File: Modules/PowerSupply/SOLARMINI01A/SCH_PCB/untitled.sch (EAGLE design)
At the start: 28 parts, among them X2 SROUB3M, X3 SROUB3M, X4 SROUB3M, X5 SROUB3M

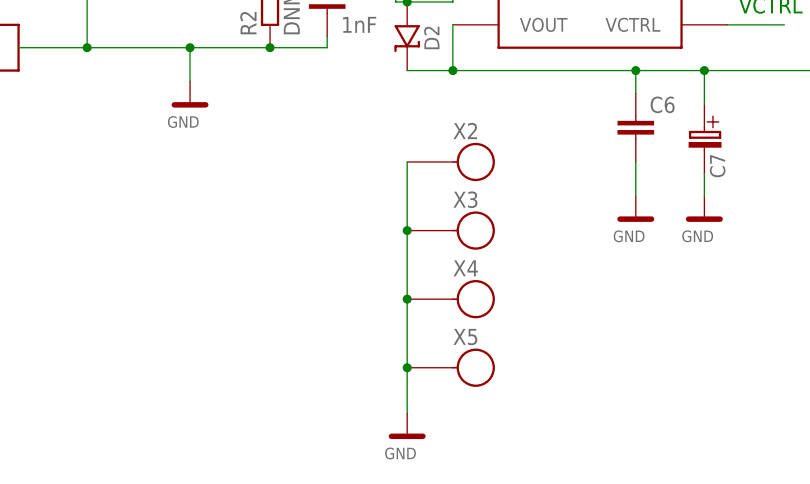
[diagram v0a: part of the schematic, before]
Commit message: 
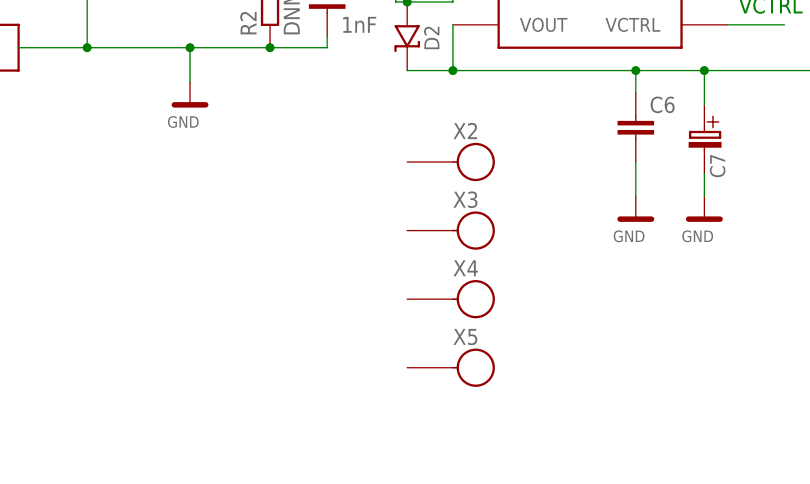
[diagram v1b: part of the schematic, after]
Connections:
- net GND: no longer X2.P$1, X3.P$1, X4.P$1, X5.P$1
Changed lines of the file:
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@@
 <?xml version="1.0" encoding="utf-8"?>
 <!DOCTYPE eagle SYSTEM "eagle.dtd">
-<eagle version="6.2">
+<eagle version="6.1">
 <drawing>
 <settings>
@@
 <part name="X4" library="moje" deviceset="SROUB3M" device=""/>
 <part name="X5" library="moje" deviceset="SROUB3M" device=""/>
-<part name="GND8" library="moje" deviceset="GND" device=""/>
 <part name="R6" library="moje_R" deviceset="R1206" device="" value="0R"/>
 <part name="R3" library="moje_R" deviceset="R1206" device="" value="0R"/>
@@
 <instance part="X4" gate="P4" x="-12.7" y="5.08"/>
 <instance part="X5" gate="P4" x="-12.7" y="-2.54"/>
-<instance part="GND8" gate="G$1" x="-20.32" y="-7.62"/>
 <instance part="R6" gate="G$1" x="55.88" y="35.56"/>
 <instance part="R3" gate="G$1" x="0" y="60.96"/>
@@
 </segment>
 <segment>
-<pinref part="X2" gate="P4" pin="P$1"/>
-<wire x1="-20.32" y1="20.32" x2="-20.32" y2="12.7" width="0.1524" layer="91"/>
-<pinref part="X3" gate="P4" pin="P$1"/>
-<junction x="-20.32" y="12.7"/>
-<wire x1="-20.32" y1="12.7" x2="-20.32" y2="5.08" width="0.1524" layer="91"/>
-<pinref part="X4" gate="P4" pin="P$1"/>
-<junction x="-20.32" y="5.08"/>
-<wire x1="-20.32" y1="5.08" x2="-20.32" y2="-2.54" width="0.1524" layer="91"/>
-<pinref part="X5" gate="P4" pin="P$1"/>
-<junction x="-20.32" y="-2.54"/>
-<wire x1="-20.32" y1="-2.54" x2="-20.32" y2="-7.62" width="0.1524" layer="91"/>
-<pinref part="GND8" gate="G$1" pin="GND"/>
-</segment>
-<segment>

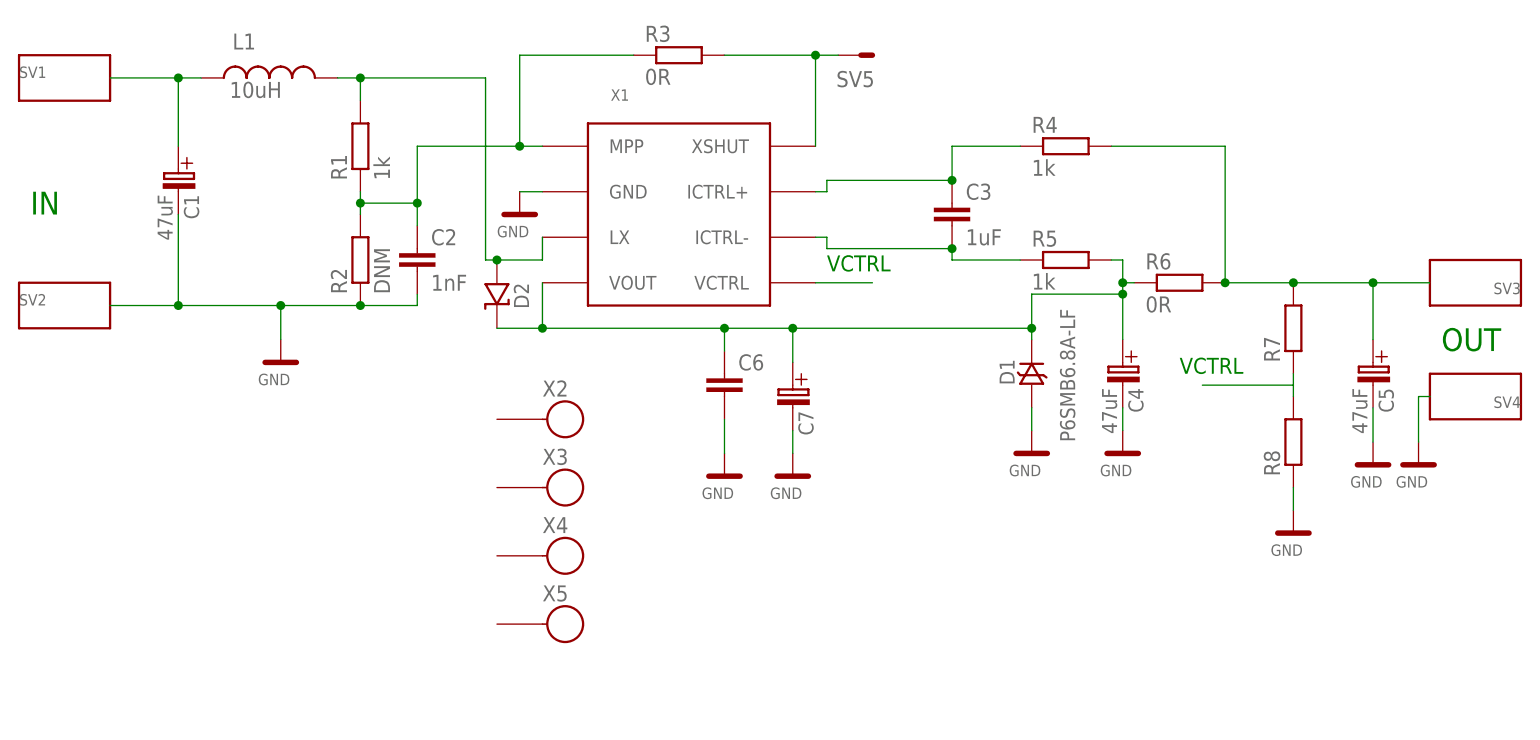
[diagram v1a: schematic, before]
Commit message: 
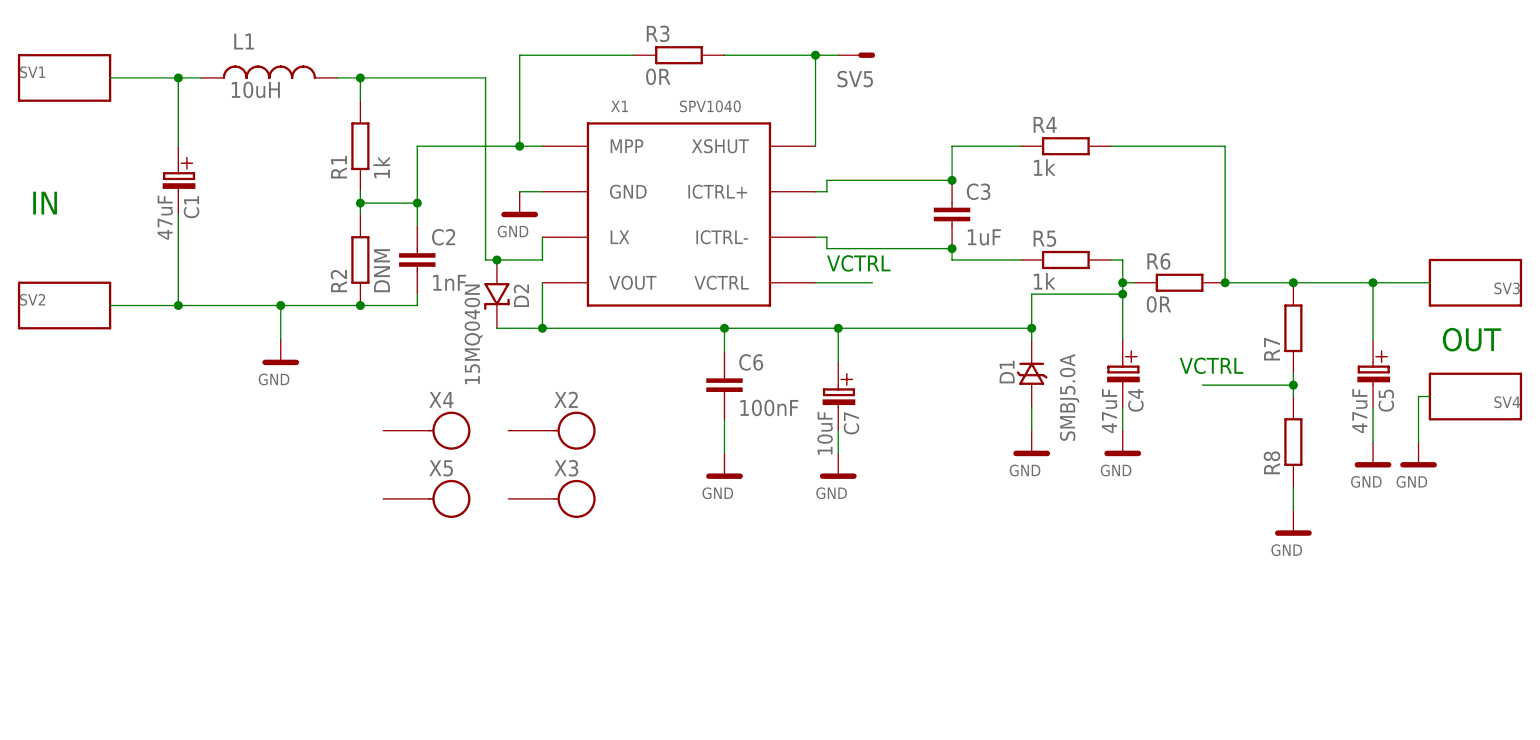
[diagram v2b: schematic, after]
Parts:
- C6: value (none) -> 100nF
- C7: value (none) -> 10uF
- D1: value P6SMB6.8A-LF -> SMBJ5.0A
- D2: value (none) -> 15MQ040N
- X1: value (none) -> SPV1040
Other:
- moved on the sheet: C7, X2, X3, X4, X5
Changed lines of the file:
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@@
 <setting verticaltext="up"/>
 </settings>
-<grid distance="0.1" unitdist="inch" unit="inch" style="lines" multiple="1" display="no" altdistance="0.01" altunitdist="inch" altunit="inch"/>
+<grid distance="0.05" unitdist="inch" unit="inch" style="lines" multiple="1" display="no" altdistance="0.01" altunitdist="inch" altunit="inch"/>
 <layers>
 <layer number="1" name="Top" color="4" fill="1" visible="no" active="no"/>
@@
 </classes>
 <parts>
-<part name="X1" library="moje_io" deviceset="SPV1040" device=""/>
+<part name="X1" library="moje_io" deviceset="SPV1040" device="" value="SPV1040"/>
 <part name="C1" library="moje_C" deviceset="C" device="" value="47uF"/>
 <part name="C2" library="moje_C" deviceset="C0805" device="" value="1nF"/>
@@
 <part name="R7" library="moje_R" deviceset="R0805" device=""/>
 <part name="R8" library="moje_R" deviceset="R0805" device=""/>
-<part name="D1" library="moje_diody" deviceset="D-TRANSIL" device="" value="P6SMB6.8A-LF"/>
+<part name="D1" library="moje_diody" deviceset="D-TRANSIL" device="" value="SMBJ5.0A"/>
 <part name="L1" library="moje_L" deviceset="DE1205-10" device="" value="10uH"/>
 <part name="SV1" library="moje_konektory" deviceset="WAGO256" device=""/>
@@
 <part name="R6" library="moje_R" deviceset="R1206" device="" value="0R"/>
 <part name="R3" library="moje_R" deviceset="R1206" device="" value="0R"/>
-<part name="D2" library="moje_diody" deviceset="D-SHOTKY-SMA" device=""/>
-<part name="C6" library="moje_C" deviceset="C0805" device=""/>
-<part name="C7" library="moje_C" deviceset="B" device=""/>
+<part name="D2" library="moje_diody" deviceset="D-SHOTKY-SMA" device="" value="15MQ040N"/>
+<part name="C6" library="moje_C" deviceset="C0805" device="" value="100nF"/>
+<part name="C7" library="moje_C" deviceset="B" device="" value="10uF"/>
 <part name="GND9" library="moje" deviceset="GND" device=""/>
 <part name="GND10" library="moje" deviceset="GND" device=""/>
@@
 </plain>
 <instances>
-<instance part="X1" gate="G$1" x="-5.08" y="45.72"/>
+<instance part="X1" gate="G$1" x="-5.08" y="45.72" smashed="yes">
+<attribute name="NAME" x="-7.62" y="54.61" size="1.27" layer="95"/>
+<attribute name="VALUE" x="0" y="54.61" size="1.27" layer="96"/>
+</instance>
 <instance part="C1" gate="G$1" x="-55.88" y="46.99" rot="R270"/>
 <instance part="C2" gate="G$1" x="-29.21" y="36.83"/>
@@
 <instance part="GND6" gate="G$1" x="77.47" y="17.78"/>
 <instance part="GND7" gate="G$1" x="82.55" y="17.78"/>
-<instance part="X2" gate="P4" x="-12.7" y="20.32"/>
-<instance part="X3" gate="P4" x="-12.7" y="12.7"/>
-<instance part="X4" gate="P4" x="-12.7" y="5.08"/>
-<instance part="X5" gate="P4" x="-12.7" y="-2.54"/>
+<instance part="X2" gate="P4" x="-11.43" y="19.05"/>
+<instance part="X3" gate="P4" x="-11.43" y="11.43"/>
+<instance part="X4" gate="P4" x="-25.4" y="19.05"/>
+<instance part="X5" gate="P4" x="-25.4" y="11.43"/>
 <instance part="R6" gate="G$1" x="55.88" y="35.56"/>
 <instance part="R3" gate="G$1" x="0" y="60.96"/>
 <instance part="D2" gate="G$1" x="-20.32" y="35.56" rot="R270"/>
 <instance part="C6" gate="G$1" x="5.08" y="22.86"/>
-<instance part="C7" gate="G$1" x="12.7" y="22.86" rot="R270"/>
+<instance part="C7" gate="G$1" x="17.78" y="22.86" rot="R270"/>
 <instance part="GND9" gate="G$1" x="5.08" y="16.51"/>
-<instance part="GND10" gate="G$1" x="12.7" y="16.51"/>
+<instance part="GND10" gate="G$1" x="17.78" y="16.51"/>
 <instance part="SV5" gate="G$1" x="17.78" y="60.96" rot="R180"/>
 </instances>
@@
 <pinref part="C7" gate="G$1" pin="C_EL-"/>
 <pinref part="GND10" gate="G$1" pin="GND"/>
-<wire x1="12.7" y1="16.51" x2="12.7" y2="19.05" width="0.1524" layer="91"/>
+<wire x1="17.78" y1="16.51" x2="17.78" y2="19.05" width="0.1524" layer="91"/>
 </segment>
 </net>
@@
 <wire x1="-15.24" y1="30.48" x2="5.08" y2="30.48" width="0.1524" layer="91"/>
 <pinref part="D1" gate="G$1" pin="K"/>
-<wire x1="5.08" y1="30.48" x2="12.7" y2="30.48" width="0.1524" layer="91"/>
-<wire x1="12.7" y1="30.48" x2="39.37" y2="30.48" width="0.1524" layer="91"/>
+<wire x1="5.08" y1="30.48" x2="17.78" y2="30.48" width="0.1524" layer="91"/>
+<wire x1="17.78" y1="30.48" x2="39.37" y2="30.48" width="0.1524" layer="91"/>
 <wire x1="39.37" y1="29.21" x2="39.37" y2="30.48" width="0.1524" layer="91"/>
 <pinref part="C4" gate="G$1" pin="C_EL+"/>
@@
 <wire x1="5.08" y1="27.94" x2="5.08" y2="30.48" width="0.1524" layer="91"/>
 <pinref part="C7" gate="G$1" pin="C_EL+"/>
-<wire x1="12.7" y1="26.67" x2="12.7" y2="30.48" width="0.1524" layer="91"/>
+<wire x1="17.78" y1="26.67" x2="17.78" y2="30.48" width="0.1524" layer="91"/>
 <junction x="5.08" y="30.48"/>
-<junction x="12.7" y="30.48"/>
+<junction x="17.78" y="30.48"/>
 </segment>
 </net>
@@
 <wire x1="68.58" y1="24.13" x2="68.58" y2="22.86" width="0.1524" layer="91"/>
 <wire x1="68.58" y1="24.13" x2="58.42" y2="24.13" width="0.1524" layer="91"/>
-</segment>
-</net>
+<junction x="68.58" y="24.13"/>
+</segment>
+</net>

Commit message: 
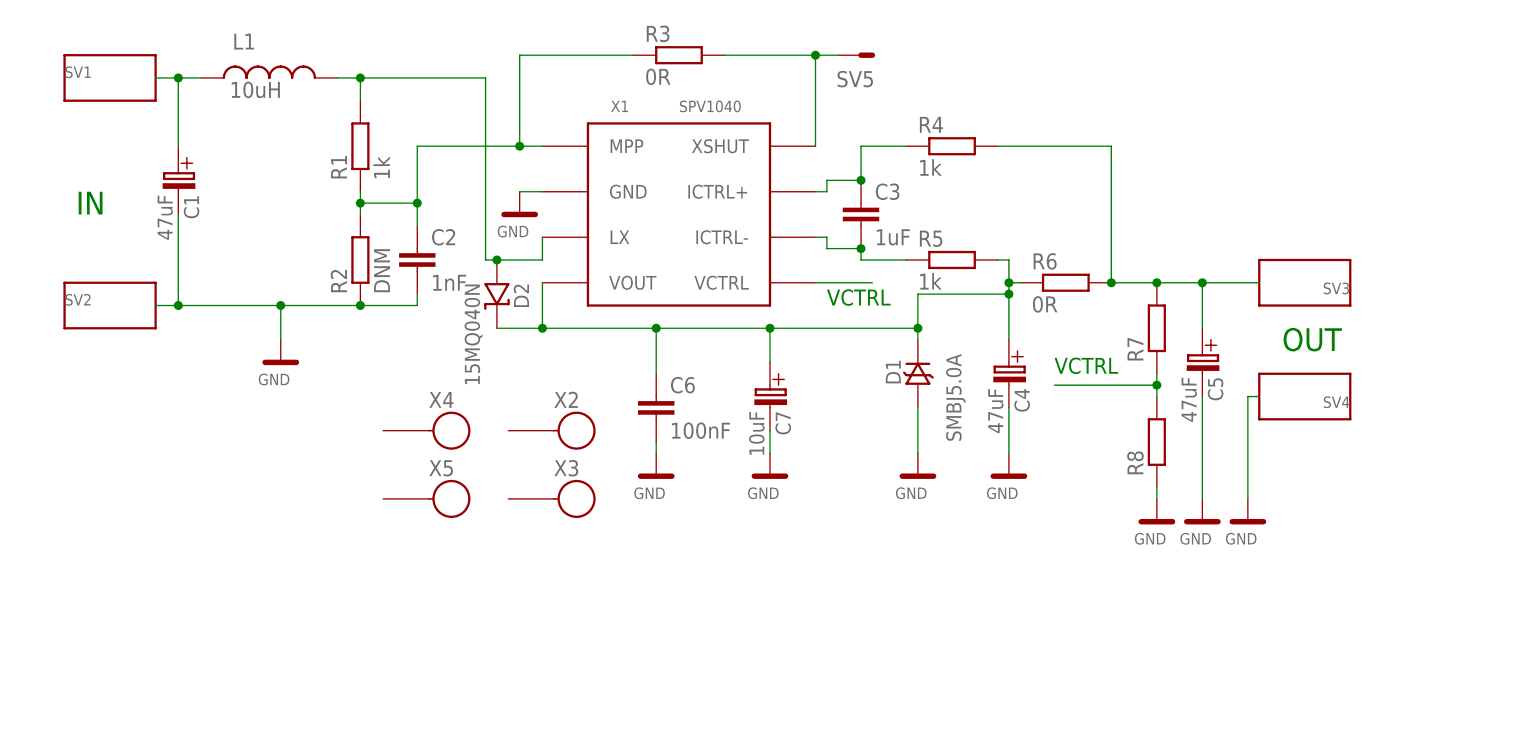
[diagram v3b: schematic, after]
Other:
- moved on the sheet: C3, C4, C5, C6, C7, D1, R4, R5, R6, R7, R8, SV1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

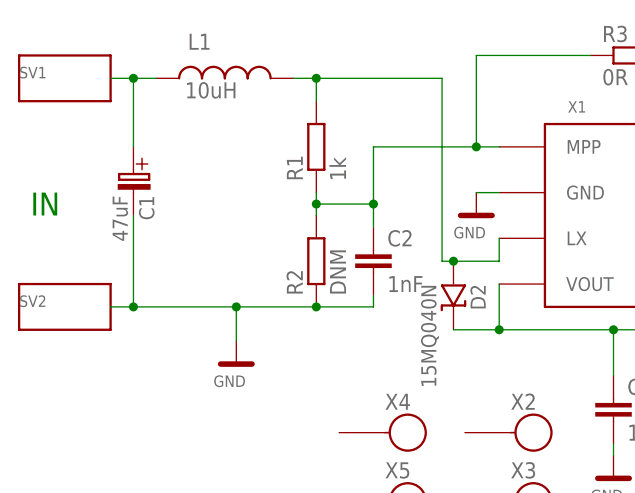
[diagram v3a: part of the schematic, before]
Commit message: 
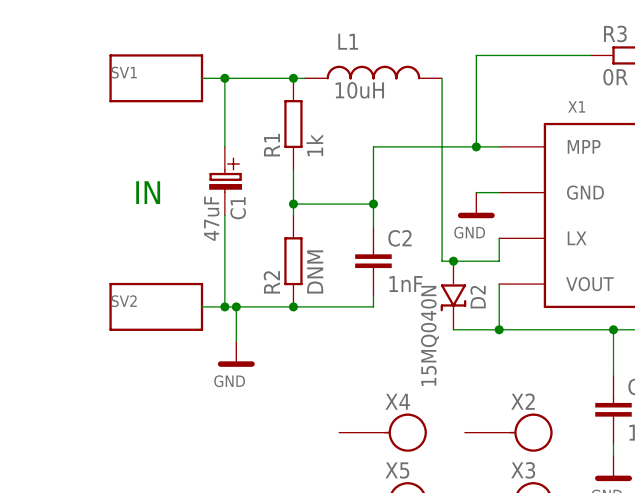
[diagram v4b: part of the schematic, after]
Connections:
- net N$1: now also R1.2
- net N$6: no longer R1.2
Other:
- moved on the sheet: C1, L1, R1, R2, SV1, SV2
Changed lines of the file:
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@@
 <text x="16.51" y="33.02" size="1.778" layer="91">VCTRL</text>
 <text x="41.91" y="25.4" size="1.778" layer="91">VCTRL</text>
-<text x="-67.31" y="43.18" size="2.54" layer="91">IN</text>
+<text x="-55.88" y="44.45" size="2.54" layer="91">IN</text>
 <text x="67.31" y="27.94" size="2.54" layer="91">OUT</text>
 </plain>
@@
 <attribute name="VALUE" x="0" y="54.61" size="1.27" layer="96"/>
 </instance>
-<instance part="C1" gate="G$1" x="-55.88" y="46.99" rot="R270"/>
+<instance part="C1" gate="G$1" x="-45.72" y="46.99" rot="R270"/>
 <instance part="C2" gate="G$1" x="-29.21" y="36.83"/>
 <instance part="C3" gate="G$1" x="20.32" y="41.91"/>
 <instance part="C4" gate="G$1" x="36.83" y="25.4" rot="R270"/>
 <instance part="C5" gate="G$1" x="58.42" y="26.67" rot="R270"/>
-<instance part="R1" gate="G$1" x="-35.56" y="50.8" rot="R90"/>
-<instance part="R2" gate="G$1" x="-35.56" y="38.1" rot="R90"/>
+<instance part="R1" gate="G$1" x="-38.1" y="53.34" rot="R90"/>
+<instance part="R2" gate="G$1" x="-38.1" y="38.1" rot="R90"/>
 <instance part="R4" gate="G$1" x="30.48" y="50.8"/>
 <instance part="R5" gate="G$1" x="30.48" y="38.1"/>
@@
 <attribute name="NAME" x="24.765" y="24.13" size="1.6764" layer="95" rot="R90"/>
 </instance>
-<instance part="L1" gate="G$1" x="-45.72" y="58.42"/>
-<instance part="SV1" gate="G$1" x="-66.04" y="58.42"/>
-<instance part="SV2" gate="G$1" x="-66.04" y="33.02"/>
+<instance part="L1" gate="G$1" x="-29.21" y="58.42"/>
+<instance part="SV1" gate="G$1" x="-55.88" y="58.42"/>
+<instance part="SV2" gate="G$1" x="-55.88" y="33.02"/>
 <instance part="SV3" gate="G$1" x="72.39" y="35.56" rot="R180"/>
 <instance part="SV4" gate="G$1" x="72.39" y="22.86" rot="R180"/>
@@
 <pinref part="SV1" gate="G$1" pin="P$1"/>
 <pinref part="L1" gate="G$1" pin="1"/>
-<wire x1="-58.42" y1="58.42" x2="-55.88" y2="58.42" width="0.1524" layer="91"/>
-<wire x1="-55.88" y1="58.42" x2="-53.34" y2="58.42" width="0.1524" layer="91"/>
-<wire x1="-55.88" y1="50.8" x2="-55.88" y2="58.42" width="0.1524" layer="91"/>
+<wire x1="-48.26" y1="58.42" x2="-45.72" y2="58.42" width="0.1524" layer="91"/>
+<wire x1="-45.72" y1="58.42" x2="-38.1" y2="58.42" width="0.1524" layer="91"/>
+<wire x1="-38.1" y1="58.42" x2="-36.83" y2="58.42" width="0.1524" layer="91"/>
+<wire x1="-45.72" y1="50.8" x2="-45.72" y2="58.42" width="0.1524" layer="91"/>
 <pinref part="C1" gate="G$1" pin="C_EL+"/>
-<junction x="-55.88" y="58.42"/>
+<junction x="-45.72" y="58.42"/>
+<pinref part="R1" gate="G$1" pin="2"/>
+<junction x="-38.1" y="58.42"/>
 </segment>
 </net>
@@
 <pinref part="R2" gate="G$1" pin="2"/>
 <pinref part="R1" gate="G$1" pin="1"/>
-<wire x1="-35.56" y1="43.18" x2="-35.56" y2="44.45" width="0.1524" layer="91"/>
+<wire x1="-38.1" y1="43.18" x2="-38.1" y2="44.45" width="0.1524" layer="91"/>
 <pinref part="C2" gate="G$1" pin="1"/>
-<wire x1="-35.56" y1="44.45" x2="-35.56" y2="45.72" width="0.1524" layer="91"/>
+<wire x1="-38.1" y1="44.45" x2="-38.1" y2="48.26" width="0.1524" layer="91"/>
 <wire x1="-29.21" y1="41.91" x2="-29.21" y2="44.45" width="0.1524" layer="91"/>
-<wire x1="-29.21" y1="44.45" x2="-35.56" y2="44.45" width="0.1524" layer="91"/>
+<wire x1="-29.21" y1="44.45" x2="-38.1" y2="44.45" width="0.1524" layer="91"/>
 <pinref part="X1" gate="G$1" pin="MPP"/>
 <wire x1="-17.78" y1="50.8" x2="-29.21" y2="50.8" width="0.1524" layer="91"/>
 <wire x1="-29.21" y1="50.8" x2="-29.21" y2="44.45" width="0.1524" layer="91"/>
-<junction x="-35.56" y="44.45"/>
+<junction x="-38.1" y="44.45"/>
 <junction x="-29.21" y="44.45"/>
 <wire x1="-15.24" y1="50.8" x2="-17.78" y2="50.8" width="0.1524" layer="91"/>
@@
 <pinref part="SV2" gate="G$1" pin="P$1"/>
 <pinref part="R2" gate="G$1" pin="1"/>
-<wire x1="-58.42" y1="33.02" x2="-55.88" y2="33.02" width="0.1524" layer="91"/>
+<wire x1="-48.26" y1="33.02" x2="-45.72" y2="33.02" width="0.1524" layer="91"/>
 <pinref part="C1" gate="G$1" pin="C_EL-"/>
-<wire x1="-55.88" y1="33.02" x2="-44.45" y2="33.02" width="0.1524" layer="91"/>
-<wire x1="-44.45" y1="33.02" x2="-35.56" y2="33.02" width="0.1524" layer="91"/>
-<wire x1="-55.88" y1="43.18" x2="-55.88" y2="33.02" width="0.1524" layer="91"/>
+<wire x1="-45.72" y1="33.02" x2="-44.45" y2="33.02" width="0.1524" layer="91"/>
+<wire x1="-44.45" y1="33.02" x2="-38.1" y2="33.02" width="0.1524" layer="91"/>
+<wire x1="-45.72" y1="43.18" x2="-45.72" y2="33.02" width="0.1524" layer="91"/>
 <pinref part="C2" gate="G$1" pin="2"/>
-<wire x1="-35.56" y1="33.02" x2="-29.21" y2="33.02" width="0.1524" layer="91"/>
+<wire x1="-38.1" y1="33.02" x2="-29.21" y2="33.02" width="0.1524" layer="91"/>
 <wire x1="-29.21" y1="33.02" x2="-29.21" y2="34.29" width="0.1524" layer="91"/>
-<junction x="-55.88" y="33.02"/>
+<junction x="-45.72" y="33.02"/>
 <junction x="-44.45" y="33.02"/>
-<junction x="-35.56" y="33.02"/>
+<junction x="-38.1" y="33.02"/>
 </segment>
 <segment>
@@
 <net name="N$6" class="0">
 <segment>
-<pinref part="L1" gate="G$1" pin="2"/>
-<pinref part="R1" gate="G$1" pin="2"/>
-<wire x1="-38.1" y1="58.42" x2="-35.56" y2="58.42" width="0.1524" layer="91"/>
-<wire x1="-35.56" y1="58.42" x2="-35.56" y2="55.88" width="0.1524" layer="91"/>
-<wire x1="-35.56" y1="58.42" x2="-21.59" y2="58.42" width="0.1524" layer="91"/>
 <wire x1="-21.59" y1="38.1" x2="-21.59" y2="58.42" width="0.1524" layer="91"/>
-<junction x="-35.56" y="58.42"/>
 <pinref part="X1" gate="G$1" pin="LX"/>
 <wire x1="-21.59" y1="38.1" x2="-20.32" y2="38.1" width="0.1524" layer="91"/>
@@
 <pinref part="D2" gate="G$1" pin="A"/>
 <junction x="-20.32" y="38.1"/>
+<pinref part="L1" gate="G$1" pin="2"/>
 </segment>
 </net>
